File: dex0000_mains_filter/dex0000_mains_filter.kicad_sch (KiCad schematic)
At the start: 16 parts, among them J1 Conn_01x03_Male, J2 Screw_Terminal_01x02

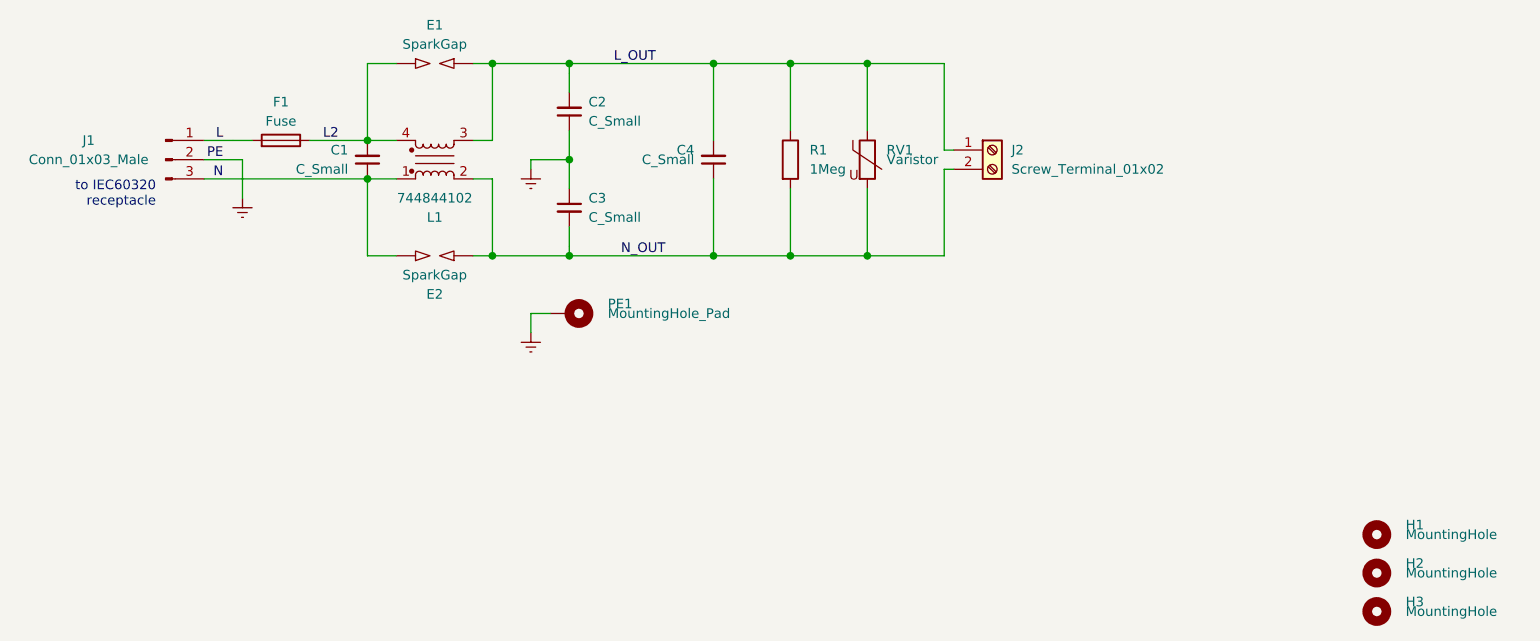
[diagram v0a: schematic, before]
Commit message: Add files via upload
updated design with documentation. Fixes 3.0mm self-clearances (now 0.75mm)
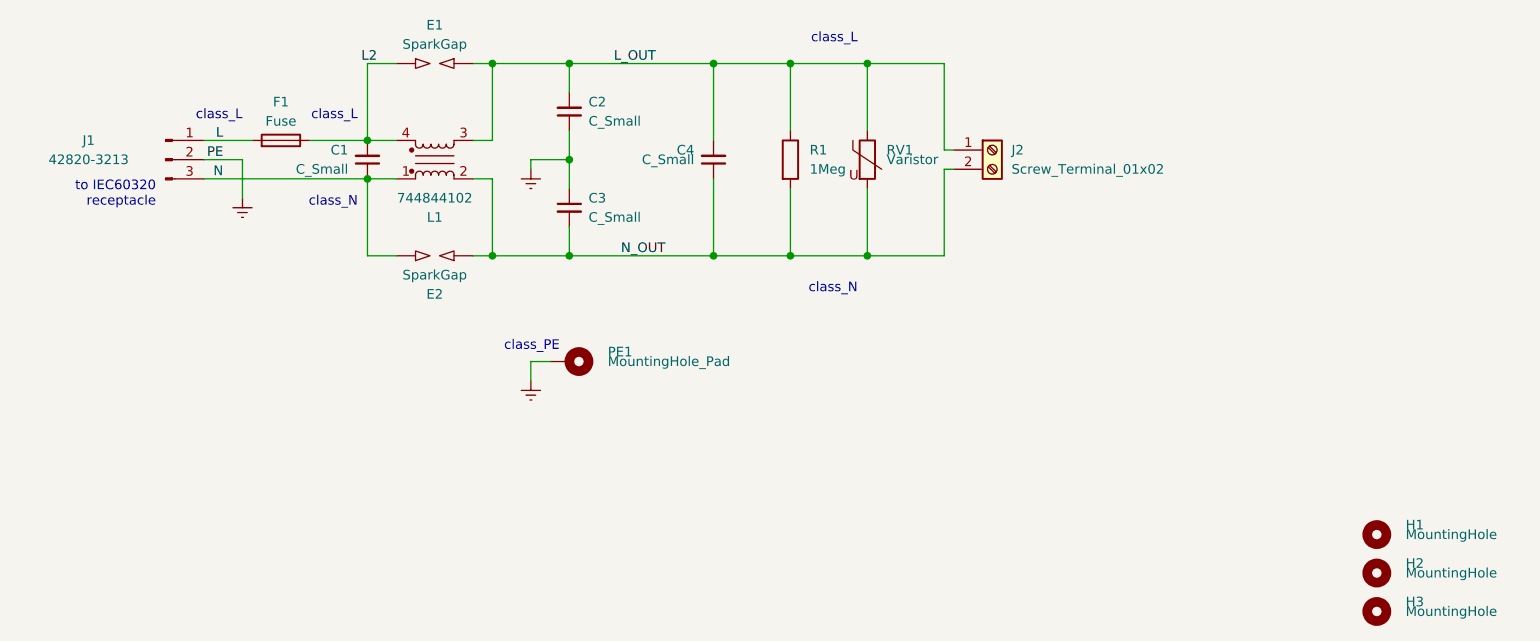
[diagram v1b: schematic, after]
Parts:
- J1: value Conn_01x03_Male -> 42820-3213
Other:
- note added: "class_L"
- note added: "class_N"
- note added: "class_PE"
- moved on the sheet: PE1
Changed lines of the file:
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@@
   (junction (at 189.23 81.28) (diameter 1.016) (color 0 0 0 0))
   (junction (at 189.23 106.68) (diameter 1.016) (color 0 0 0 0))
-  (wire (pts (xy 101.6 91.44) (xy 105.41 91.44))
+  (wire (pts (xy 101.6 91.44) (xy 107.95 91.44))
     (stroke (width 0) (type solid) (color 0 0 0 0))
   )
@@
     (stroke (width 0) (type solid) (color 0 0 0 0))
   )
-  (wire (pts (xy 105.41 91.44) (xy 107.95 91.44))
-    (stroke (width 0) (type solid) (color 0 0 0 0))
-  )
   (wire (pts (xy 106.68 93.98) (xy 106.68 99.06))
     (stroke (width 0) (type solid) (color 0 0 0 0))
@@
     (stroke (width 0) (type solid) (color 0 0 0 0))
   )
-  (wire (pts (xy 144.78 114.3) (xy 144.78 116.84))
-    (stroke (width 0) (type solid) (color 0 0 0 0))
-  )
-  (wire (pts (xy 144.78 114.3) (xy 147.32 114.3))
-    (stroke (width 0) (type solid) (color 0 0 0 0))
-  )
-  (wire (pts (xy 149.86 81.28) (xy 149.86 82.55))
+  (wire (pts (xy 144.78 120.65) (xy 144.78 123.19))
+    (stroke (width 0) (type solid) (color 0 0 0 0))
+  )
+  (wire (pts (xy 144.78 120.65) (xy 147.32 120.65))
+    (stroke (width 0) (type solid) (color 0 0 0 0))
+  )
+  (wire (pts (xy 149.86 81.28) (xy 149.86 85.09))
     (stroke (width 0) (type solid) (color 0 0 0 0))
   )
@@
     (stroke (width 0) (type solid) (color 0 0 0 0))
   )
-  (wire (pts (xy 149.86 82.55) (xy 149.86 85.09))
-    (stroke (width 0) (type solid) (color 0 0 0 0))
-  )
   (wire (pts (xy 149.86 93.98) (xy 149.86 90.17))
     (stroke (width 0) (type solid) (color 0 0 0 0))
@@
     (stroke (width 0) (type solid) (color 0 0 0 0))
   )
-  (wire (pts (xy 149.86 105.41) (xy 149.86 102.87))
-    (stroke (width 0) (type solid) (color 0 0 0 0))
-  )
-  (wire (pts (xy 149.86 105.41) (xy 149.86 106.68))
+  (wire (pts (xy 149.86 102.87) (xy 149.86 106.68))
     (stroke (width 0) (type solid) (color 0 0 0 0))
   )
@@
     (effects (font (size 1.27 1.27)) (justify right bottom))
   )
+  (text "class_L" (at 106.68 88.9 180)
+    (effects (font (size 1.27 1.27)) (justify right bottom))
+  )
+  (text "class_L" (at 121.92 88.9 180)
+    (effects (font (size 1.27 1.27)) (justify right bottom))
+  )
+  (text "class_N" (at 121.92 100.33 180)
+    (effects (font (size 1.27 1.27)) (justify right bottom))
+  )
+  (text "class_PE" (at 148.59 119.38 180)
+    (effects (font (size 1.27 1.27)) (justify right bottom))
+  )
+  (text "class_L" (at 187.96 78.74 180)
+    (effects (font (size 1.27 1.27)) (justify right bottom))
+  )
+  (text "class_N" (at 187.96 111.76 180)
+    (effects (font (size 1.27 1.27)) (justify right bottom))
+  )
   (label "L" (at 104.14 91.44 180)
     (effects (font (size 1.27 1.27)) (justify right bottom))
@@
     (effects (font (size 1.27 1.27)) (justify right bottom))
   )
-  (label "L2" (at 119.38 91.44 180)
+  (label "L2" (at 124.46 81.28 180)
     (effects (font (size 1.27 1.27)) (justify right bottom))
   )
@@
     )
   )
-  (symbol (lib_id "power:Earth") (at 144.78 116.84 0) (unit 1)
-    (in_bom yes) (on_board yes)
-    (property "Reference" "#PWR03" (id 0) (at 144.78 123.19 0)
-      (effects (font (size 1.27 1.27)) hide)
-    )
-    (property "Value" "Earth" (id 1) (at 144.78 120.65 0)
-      (effects (font (size 1.27 1.27)) hide)
-    )
-    (property "Footprint" "" (id 2) (at 144.78 116.84 0)
-      (effects (font (size 1.27 1.27)) hide)
-    )
-    (property "Datasheet" "~" (id 3) (at 144.78 116.84 0)
+  (symbol (lib_id "power:Earth") (at 144.78 123.19 0) (unit 1)
+    (in_bom yes) (on_board yes)
+    (property "Reference" "#PWR03" (id 0) (at 144.78 129.54 0)
+      (effects (font (size 1.27 1.27)) hide)
+    )
+    (property "Value" "Earth" (id 1) (at 144.78 127 0)
+      (effects (font (size 1.27 1.27)) hide)
+    )
+    (property "Footprint" "" (id 2) (at 144.78 123.19 0)
+      (effects (font (size 1.27 1.27)) hide)
+    )
+    (property "Datasheet" "~" (id 3) (at 144.78 123.19 0)
       (effects (font (size 1.27 1.27)) hide)
     )
@@
     )
   )
-  (symbol (lib_id "Mechanical:MountingHole_Pad") (at 149.86 114.3 270) (unit 1)
-    (in_bom yes) (on_board yes)
-    (property "Reference" "PE1" (id 0) (at 154.94 113.03 90)
-      (effects (font (size 1.27 1.27)) (justify left))
-    )
-    (property "Value" "MountingHole_Pad" (id 1) (at 154.94 114.3 90)
-      (effects (font (size 1.27 1.27)) (justify left))
-    )
-    (property "Footprint" "MountingHole:MountingHole_4.3mm_M4_Pad_Via" (id 2) (at 149.86 114.3 0)
-      (effects (font (size 1.27 1.27)) hide)
-    )
-    (property "Datasheet" "~" (id 3) (at 149.86 114.3 0)
+  (symbol (lib_id "Mechanical:MountingHole_Pad") (at 149.86 120.65 270) (unit 1)
+    (in_bom yes) (on_board yes)
+    (property "Reference" "PE1" (id 0) (at 154.94 119.38 90)
+      (effects (font (size 1.27 1.27)) (justify left))
+    )
+    (property "Value" "MountingHole_Pad" (id 1) (at 154.94 120.65 90)
+      (effects (font (size 1.27 1.27)) (justify left))
+    )
+    (property "Footprint" "MountingHole:MountingHole_4.3mm_M4_Pad_Via" (id 2) (at 149.86 120.65 0)
+      (effects (font (size 1.27 1.27)) hide)
+    )
+    (property "Datasheet" "~" (id 3) (at 149.86 120.65 0)
       (effects (font (size 1.27 1.27)) hide)
     )
@@
     (in_bom yes) (on_board yes)
     (property "Reference" "J1" (id 0) (at 86.36 91.44 0))
-    (property "Value" "Conn_01x03_Male" (id 1) (at 86.36 93.98 0))
+    (property "Value" "42820-3213" (id 1) (at 86.36 93.98 0))
     (property "Footprint" "Connector_Molex:Molex_Mini-Fit_Sr_42820-32XX_1x03_P10.00mm_Horizontal_ThermalVias" (id 2) (at 96.52 93.98 0)
       (effects (font (size 1.27 1.27)) hide)
@@
     )
     (path "/3fbb6a52-7330-4e47-bd85-5d54abcbd092"
-      (reference "J1") (unit 1) (value "Conn_01x03_Male") (footprint "Connector_Molex:Molex_Mini-Fit_Sr_42820-32XX_1x03_P10.00mm_Horizontal_ThermalVias")
+      (reference "J1") (unit 1) (value "42820-3213") (footprint "Connector_Molex:Molex_Mini-Fit_Sr_42820-32XX_1x03_P10.00mm_Horizontal_ThermalVias")
     )
     (path "/ea43d38a-7077-413c-b8ba-3e2f263fc87c"
